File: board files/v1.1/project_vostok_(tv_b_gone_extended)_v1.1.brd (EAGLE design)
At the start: 100 x 44 mm, 29 parts, among them IC1 ATMEGA644PV-10PU, IC2 MCP1825S-3302E_DB, Q5 MPS2907A, T1 2N3904, T2 2N3904, T3 2N3904, T4 2N3904, U1 PEC11R-4015F-S0024

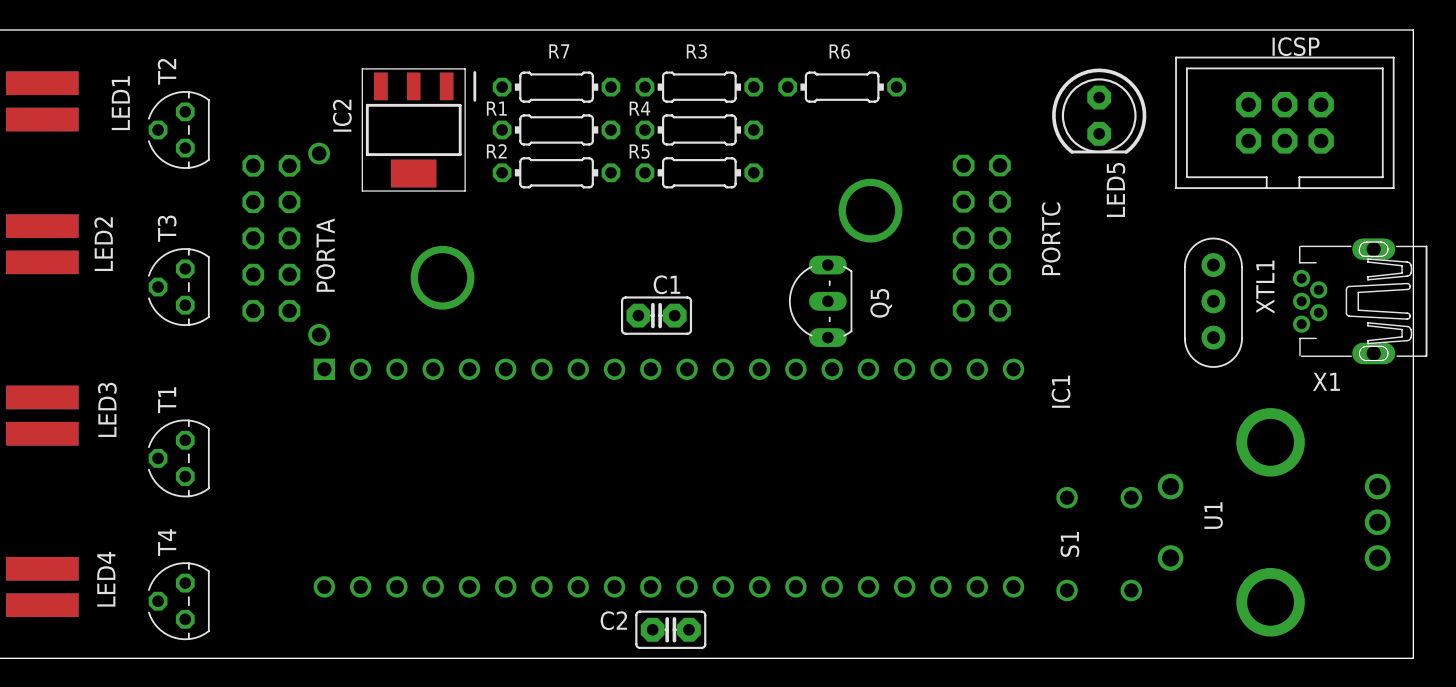
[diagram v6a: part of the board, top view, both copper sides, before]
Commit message: modify labels for board
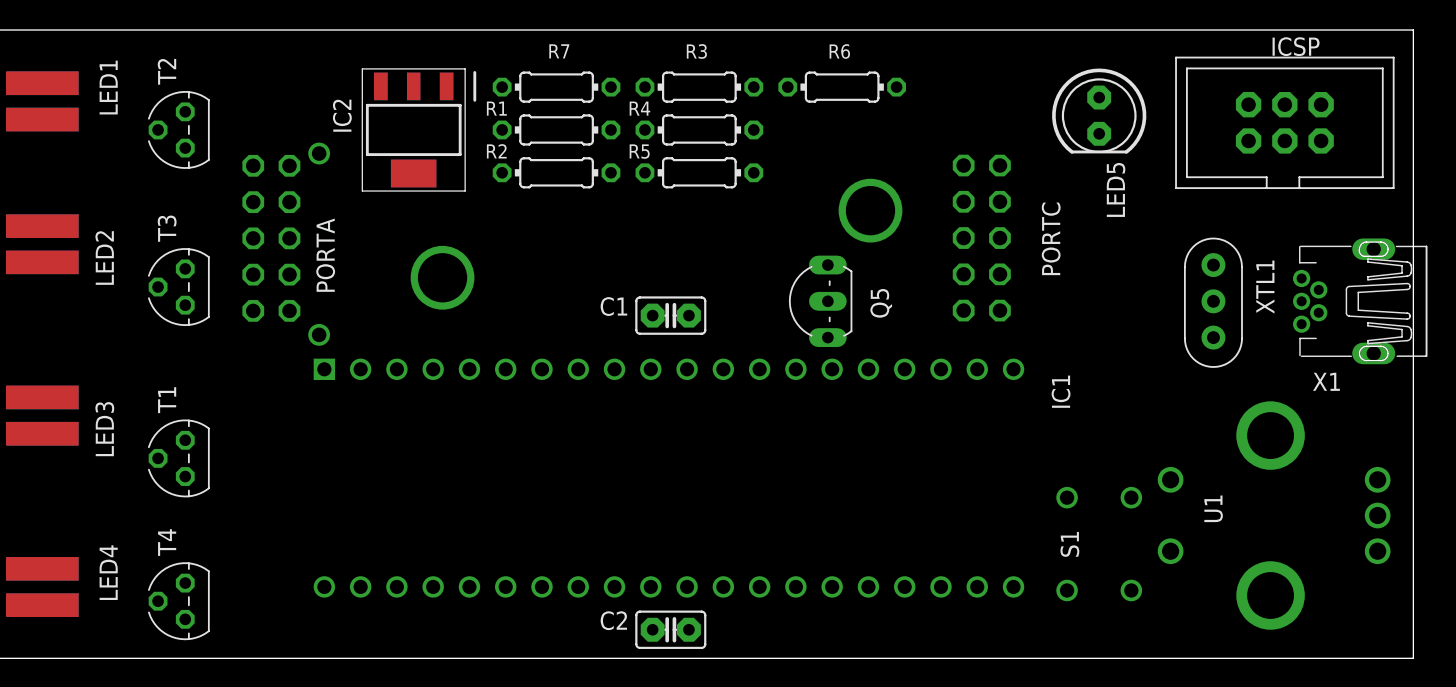
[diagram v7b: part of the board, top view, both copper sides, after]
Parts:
- moved C1 1.00 mm to (48.0, 24.0)
- moved U1 0.47 mm to (90.0, 10.0)
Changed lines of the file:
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@@
 <attribute name="NAME" x="62" y="26" size="1.27" layer="25" ratio="10" rot="R270"/>
 </element>
-<element name="LED3" library="tvbgone" package="5MM-SIDE" value="LED" x="4" y="17" rot="MR270">
-<attribute name="NAME" x="9.1816" y="15.349" size="1.27" layer="25" ratio="10" rot="R90"/>
-<attribute name="VALUE" x="4.6096" y="13.9774" size="1.27" layer="27" ratio="10" rot="R180"/>
-</element>
-<element name="LED1" library="tvbgone" package="5MM-SIDE" value="LED" x="4" y="39" rot="MR270">
-<attribute name="NAME" x="8.8514" y="40.905" size="1.27" layer="25" ratio="10" rot="R270"/>
-<attribute name="VALUE" x="4.6096" y="36.1044" size="1.27" layer="27" ratio="10" rot="R180"/>
-</element>
-<element name="LED2" library="tvbgone" package="5MM-SIDE" value="LED" x="4" y="29" rot="MR270">
-<attribute name="NAME" x="8.9276" y="26.968" size="1.27" layer="25" ratio="10" rot="R90"/>
-<attribute name="VALUE" x="1.1044" y="24.9106" size="1.27" layer="27" ratio="10"/>
+<element name="LED3" library="tvbgone" package="5MM-SIDE" value="LED" x="4" y="17" smashed="yes" rot="MR270">
+<attribute name="NAME" x="9" y="14" size="1.27" layer="25" ratio="10" rot="R90"/>
+</element>
+<element name="LED1" library="tvbgone" package="5MM-SIDE" value="LED" x="4" y="39" smashed="yes" rot="MR270">
+<attribute name="NAME" x="8" y="42" size="1.27" layer="25" ratio="10" rot="R270"/>
+</element>
+<element name="LED2" library="tvbgone" package="5MM-SIDE" value="LED" x="4" y="29" smashed="yes" rot="MR270">
+<attribute name="NAME" x="9" y="26" size="1.27" layer="25" ratio="10" rot="R90"/>
 </element>
 <element name="LED4" library="tvbgone" package="5MM-SIDE" value="LED" x="4" y="5" smashed="yes" rot="MR270">
-<attribute name="NAME" x="7.8354" y="7.54" size="1.27" layer="25" ratio="10" rot="R270"/>
+<attribute name="NAME" x="8" y="8" size="1.27" layer="25" ratio="10" rot="R270"/>
 </element>
 <element name="ICSP" library="adaprog" package="ISP6" value="PINHD-2X3THM" x="91" y="37.5" smashed="yes">
@@
 <attribute name="VALUE" x="81.5" y="28.5" size="1.27" layer="27" rot="R270"/>
 </element>
-<element name="C1" library="rcl-ez" package="C025-025X050" value="100nF" x="47" y="24" smashed="yes">
-<attribute name="NAME" x="46.714" y="25.524" size="1.27" layer="25" ratio="10"/>
-<attribute name="VALUE" x="43.206" y="27.286" size="1.27" layer="27" ratio="10" rot="R270"/>
+<element name="C1" library="rcl-ez" package="C025-025X050" value="100nF" x="48" y="24" smashed="yes">
+<attribute name="NAME" x="43" y="24" size="1.27" layer="25" ratio="10"/>
+<attribute name="VALUE" x="51" y="24" size="1.27" layer="27" ratio="10"/>
 </element>
 <element name="PORTA" library="pinhead" library_urn="urn:adsk.eagle:library:325" package="2X05" package3d_urn="urn:adsk.eagle:package:22470/2" value="" x="20.029640625" y="29.408059375" smashed="yes" rot="MR270">
@@
 <attribute name="SUPPLIER_NAME" value="RS" x="42.7" y="138.6" size="1.778" layer="27" rot="R270" display="off"/>
 </element>
-<element name="U1" library="SamacSys_Parts" package="PEC12R-4XXXF-SXXXX_1" value="PEC11R-4015F-S0024" x="90" y="9.525" smashed="yes" rot="MR270">
-<attribute name="3D_PACKAGE" value="" x="194.14" y="186.055" size="1.778" layer="28" rot="MR270" display="off"/>
-<attribute name="ALLIED_NUMBER" value="" x="194.14" y="186.055" size="1.778" layer="28" rot="MR270" display="off"/>
-<attribute name="DESCRIPTION" value="Bourns 24 Pulse Incremental Mechanical Rotary Encoder with a 6 mm Flat Shaft (Not Indexed), Through Hole" x="194.14" y="186.055" size="1.778" layer="28" rot="MR270" display="off"/>
-<attribute name="HEIGHT" value="mm" x="194.14" y="186.055" size="1.778" layer="28" rot="MR270" display="off"/>
-<attribute name="MANUFACTURER_NAME" value="Bourns" x="194.14" y="186.055" size="1.778" layer="28" rot="MR270" display="off"/>
-<attribute name="MANUFACTURER_PART_NUMBER" value="PEC11R-4015F-S0024" x="194.14" y="186.055" size="1.778" layer="28" rot="MR270" display="off"/>
-<attribute name="NAME" x="86" y="10" size="1.27" layer="25" rot="R270" align="center"/>
-<attribute name="OTHER_PART_NUMBER" value="" x="194.14" y="186.055" size="1.778" layer="28" rot="MR270" display="off"/>
-<attribute name="RS_PART_NUMBER" value="7377739P" x="194.14" y="186.055" size="1.778" layer="28" rot="MR270" display="off"/>
-<attribute name="SUPPLIER_NAME" value="RS" x="194.14" y="186.055" size="1.778" layer="28" rot="MR270" display="off"/>
+<element name="U1" library="SamacSys_Parts" package="PEC12R-4XXXF-SXXXX_1" value="PEC11R-4015F-S0024" x="90" y="10" smashed="yes" rot="MR270">
+<attribute name="3D_PACKAGE" value="" x="194.14" y="186.53" size="1.778" layer="28" rot="MR270" display="off"/>
+<attribute name="ALLIED_NUMBER" value="" x="194.14" y="186.53" size="1.778" layer="28" rot="MR270" display="off"/>
+<attribute name="DESCRIPTION" value="Bourns 24 Pulse Incremental Mechanical Rotary Encoder with a 6 mm Flat Shaft (Not Indexed), Through Hole" x="194.14" y="186.53" size="1.778" layer="28" rot="MR270" display="off"/>
+<attribute name="HEIGHT" value="mm" x="194.14" y="186.53" size="1.778" layer="28" rot="MR270" display="off"/>
+<attribute name="MANUFACTURER_NAME" value="Bourns" x="194.14" y="186.53" size="1.778" layer="28" rot="MR270" display="off"/>
+<attribute name="MANUFACTURER_PART_NUMBER" value="PEC11R-4015F-S0024" x="194.14" y="186.53" size="1.778" layer="28" rot="MR270" display="off"/>
+<attribute name="NAME" x="86" y="10.475" size="1.27" layer="25" rot="R270" align="center"/>
+<attribute name="OTHER_PART_NUMBER" value="" x="194.14" y="186.53" size="1.778" layer="28" rot="MR270" display="off"/>
+<attribute name="RS_PART_NUMBER" value="7377739P" x="194.14" y="186.53" size="1.778" layer="28" rot="MR270" display="off"/>
+<attribute name="SUPPLIER_NAME" value="RS" x="194.14" y="186.53" size="1.778" layer="28" rot="MR270" display="off"/>
 </element>
 <element name="BAT_1" library="SamacSys_Parts" package="2468" value="2468" x="47" y="29" rot="MR0">
@@
 <wire x1="92.175" y1="26.6" x2="93.54" y2="38.77" width="0" layer="19" extent="1-1"/>
 <wire x1="86" y1="25" x2="92.175" y2="26.6" width="0" layer="19" extent="1-1"/>
-<wire x1="97.5" y1="9.525" x2="92.175" y2="26.6" width="0" layer="19" extent="1-1"/>
-<wire x1="83" y1="7.025" x2="97.5" y2="9.525" width="0" layer="19" extent="1-1"/>
-<wire x1="80.25" y1="4.75" x2="83" y2="7.025" width="0" layer="19" extent="1-1"/>
+<wire x1="97.5" y1="10" x2="92.175" y2="26.6" width="0" layer="19" extent="1-1"/>
+<wire x1="83" y1="7.5" x2="97.5" y2="10" width="0" layer="19" extent="1-1"/>
+<wire x1="80.25" y1="4.75" x2="83" y2="7.5" width="0" layer="19" extent="1-1"/>
 <wire x1="75.75" y1="4.75" x2="80.25" y2="4.75" width="0" layer="19" extent="1-1"/>
 <wire x1="68.51" y1="34.51" x2="86" y2="25" width="0" layer="19" extent="1-1"/>
-<wire x1="48.27" y1="24" x2="68.51" y2="34.51" width="0" layer="19" extent="1-1"/>
-<wire x1="49.14" y1="20.24" x2="48.27" y2="24" width="0" layer="19" extent="1-1"/>
-<wire x1="49.27" y1="2" x2="48.27" y2="24" width="0" layer="19" extent="1-1"/>
+<wire x1="49.27" y1="24" x2="68.51" y2="34.51" width="0" layer="19" extent="1-1"/>
+<wire x1="49.14" y1="20.24" x2="49.27" y2="24" width="0" layer="19" extent="1-1"/>
+<wire x1="49.27" y1="2" x2="49.27" y2="24" width="0" layer="19" extent="1-1"/>
 <wire x1="46.6" y1="5" x2="49.27" y2="2" width="0" layer="19" extent="1-1"/>
 <wire x1="30" y1="33.95" x2="46.6" y2="5" width="0" layer="19" extent="1-1"/>
@@
 <contactref element="U1" pad="1"/>
 <contactref element="IC1" pad="1"/>
-<wire x1="23.74" y1="20.24" x2="97.5" y2="12.025" width="0" layer="19" extent="1-1"/>
+<wire x1="23.74" y1="20.24" x2="97.5" y2="12.5" width="0" layer="19" extent="1-1"/>
 </signal>
 <signal name="PB1">
 <contactref element="U1" pad="2"/>
 <contactref element="IC1" pad="2"/>
-<wire x1="26.28" y1="20.24" x2="97.5" y2="7.025" width="0" layer="19" extent="1-1"/>
+<wire x1="26.28" y1="20.24" x2="97.5" y2="7.5" width="0" layer="19" extent="1-1"/>
 </signal>
 <signal name="VOUT_REG">
@@
 <contactref element="PORTA" pad="1"/>
 <wire x1="71.05" y1="34.51" x2="88.46" y2="38.77" width="0" layer="19" extent="1-1"/>
-<wire x1="45.73" y1="24" x2="71.05" y2="34.51" width="0" layer="19" extent="1-1"/>
-<wire x1="46.6" y1="20.24" x2="45.73" y2="24" width="0" layer="19" extent="1-1"/>
-<wire x1="46.73" y1="2" x2="45.73" y2="24" width="0" layer="19" extent="1-1"/>
+<wire x1="46.73" y1="24" x2="71.05" y2="34.51" width="0" layer="19" extent="1-1"/>
+<wire x1="46.6" y1="20.24" x2="46.73" y2="24" width="0" layer="19" extent="1-1"/>
+<wire x1="46.73" y1="2" x2="46.73" y2="24" width="0" layer="19" extent="1-1"/>
 <wire x1="49.14" y1="5" x2="46.73" y2="2" width="0" layer="19" extent="1-1"/>
 <wire x1="46.19" y1="40" x2="49.14" y2="5" width="0" layer="19" extent="1-1"/>
@@
 <contactref element="R1" pad="1"/>
 <wire x1="36.19" y1="37" x2="59.3" y2="20.24" width="0" layer="19" extent="1-1"/>
-<wire x1="83" y1="12.025" x2="59.3" y2="20.24" width="0" layer="19" extent="1-1"/>
+<wire x1="83" y1="12.5" x2="59.3" y2="20.24" width="0" layer="19" extent="1-1"/>
 </signal>
 <signal name="N$13">

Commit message: begin wiring
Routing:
- net VOUT_REG: track 0.00 -> 103.1 mm
- net VIN_REG: track 0.00 -> 86.3 mm
- net PD1: track 0.00 -> 66.7 mm, vias 0 -> 1
- net N$4: track 0.00 -> 47.9 mm
- net RESET: track 0.00 -> 34.6 mm
- net PD0: track 0.00 -> 28.1 mm
- net N$7: track 0.00 -> 19.5 mm
